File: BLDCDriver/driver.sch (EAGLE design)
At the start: 39 parts, among them Q1 NJM7800S, U1 QFN50P400X400X100-25NDRV8300D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, U2 AS5048A-HTSP-500, U4 SOP80P620X125-8N

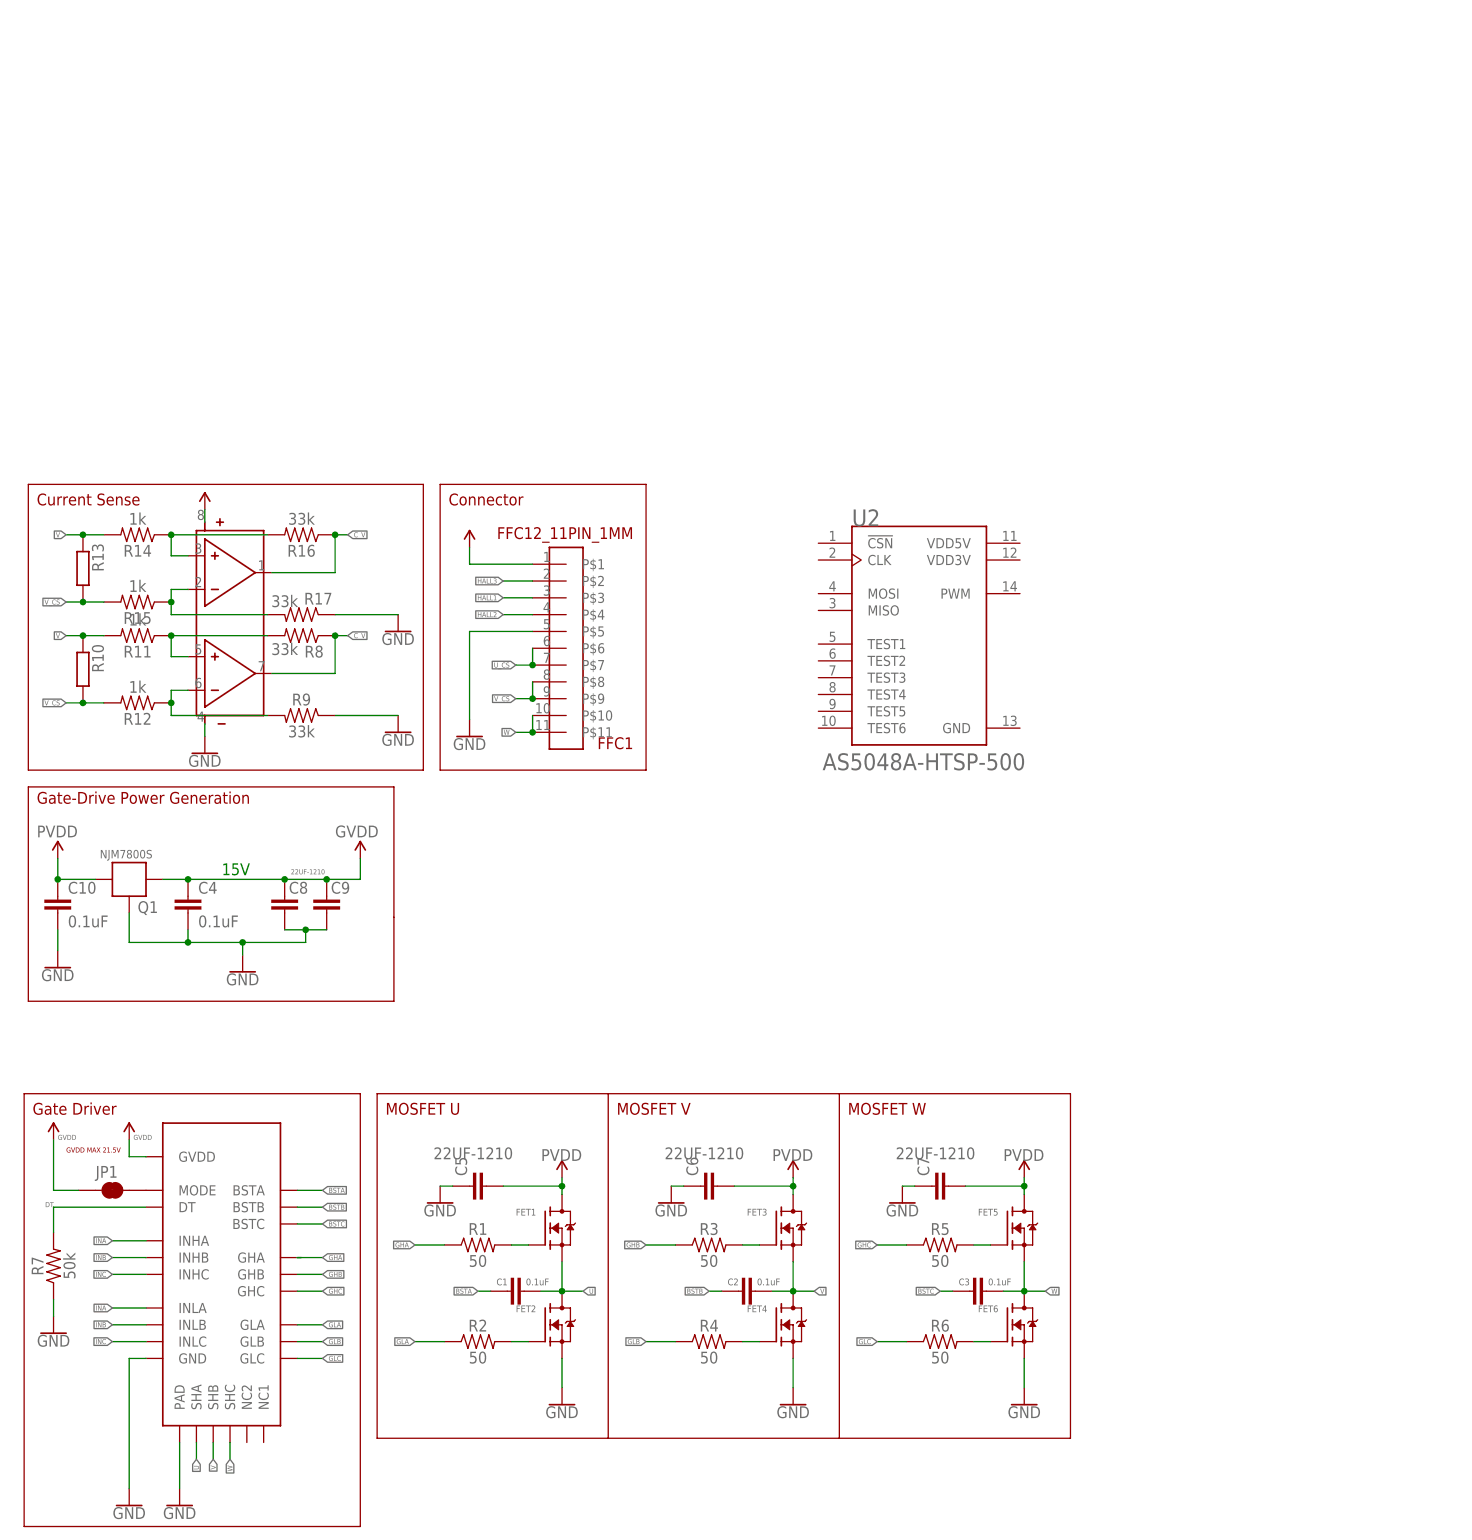
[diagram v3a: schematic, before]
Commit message: STM32と磁気エンコーダを追加した
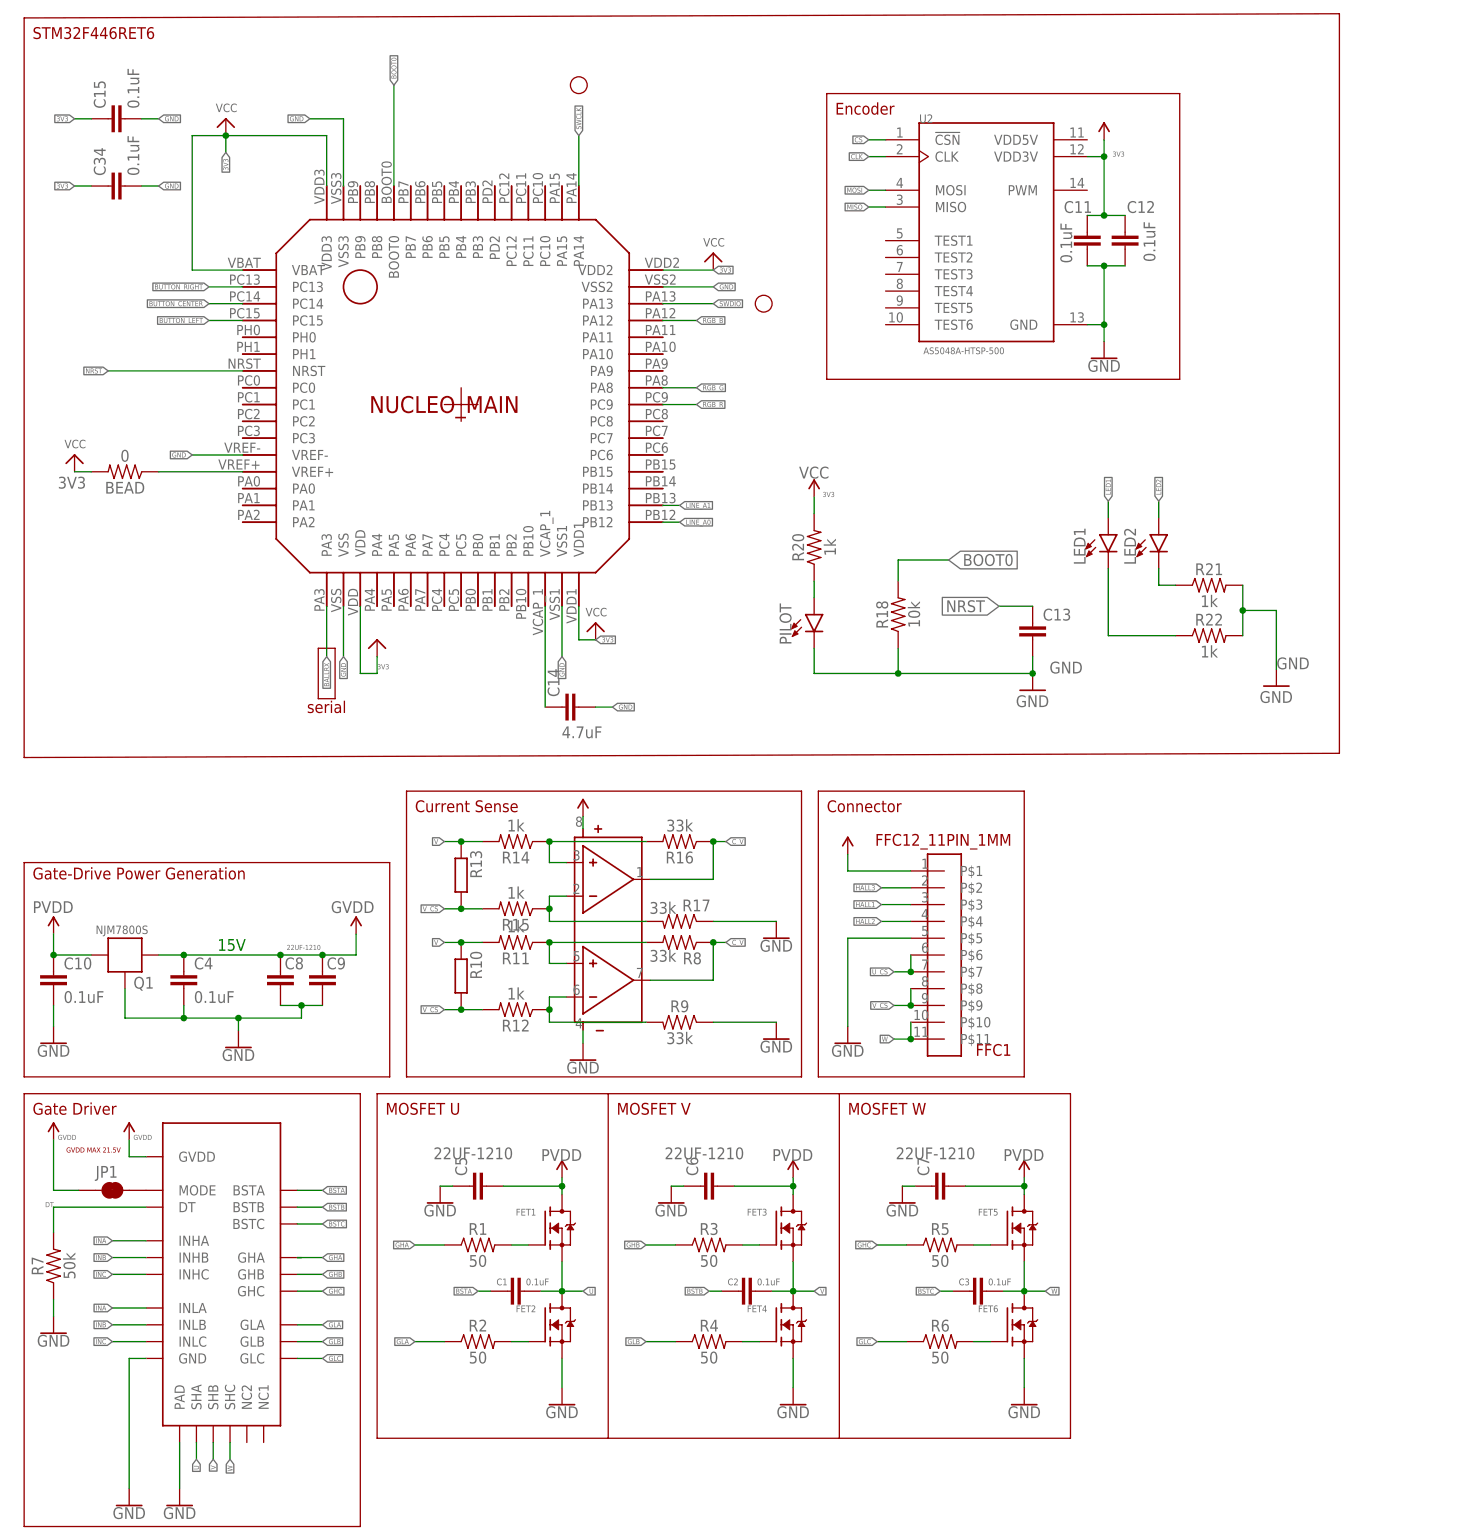
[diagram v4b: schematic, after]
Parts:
- added BEAD: 0, SparkFun-Resistors:0OHM-0603-1/10W-5%
- added C11, C12: 0.1uF, SparkFun-Capacitors:0.1UF-0603-100V-10%
- added C13: 0.1UF_1608, Custom_Designed_By_Yusei:0.1UF_1608
- added C14: 4.7uF, SparkFun-Capacitors:0.1UF-0603-25V-(+80/-20%)
- added C15, C34: 0.1uF, SparkFun-Capacitors:0.1UF-0603-25V-(+80/-20%)
- added LED1, LED2, PILOT: LED-SMD, Custom_Designed_By_Yusei:LED-SMD
- added NUCLEO_MAIN: F446RET6, STM32F446RET6:STM32F446RET6
- added R18: 10k, Custom_Designed_By_Yusei:RESISTOR-0603-1/10W-1%
- added R20, R21, R22: 1k, Custom_Designed_By_Yusei:RESISTOR-0603-1/10W-1%
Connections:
- new net BALLRX: NUCLEO_MAIN.PA3
- new net BOOT0: NUCLEO_MAIN.BOOT0, R18.2
- new net BUTTON_CENTER: NUCLEO_MAIN.PC14
- new net BUTTON_LEFT: NUCLEO_MAIN.PC15
- new net BUTTON_RIGHT: NUCLEO_MAIN.PC13
- new net CLK: U2.CLK
- new net CS: U2.!CSN
- new net LED1: LED1.A
- new net LED2: LED2.A
- new net LINE_A0: NUCLEO_MAIN.PB12
- new net LINE_A1: NUCLEO_MAIN.PB13
- new net MISO: U2.MISO
- new net MOSI: U2.MOSI
- new net N$12: LED2.C, R21.1
- new net N$13: LED1.C, R22.1
- new net NRST: C13.1, NUCLEO_MAIN.NRST
- new net POWERLED_RESISTOR: PILOT.A, R20.1
- new net RGB_B: NUCLEO_MAIN.PA12
- new net RGB_G: NUCLEO_MAIN.PA8
- new net RGB_R: NUCLEO_MAIN.PC9
- new net SWCLK: NUCLEO_MAIN.PA14
- new net SWDIO: NUCLEO_MAIN.PA13
- new net VCAP: C14.1, NUCLEO_MAIN.VCAP_1
- new net VDDA: BEAD.1, NUCLEO_MAIN.VREF+
- net 3V3: now also BEAD.2, C11.1, C12.1, C15.1, C34.1, NUCLEO_MAIN.VBAT, NUCLEO_MAIN.VDD, NUCLEO_MAIN.VDD1, NUCLEO_MAIN.VDD2, NUCLEO_MAIN.VDD3, R20.2, U2.VDD3V
- net GND: now also C11.2, C12.2, C13.2, C14.2, C15.2, C34.2, NUCLEO_MAIN.VREF-, NUCLEO_MAIN.VSS, NUCLEO_MAIN.VSS1, NUCLEO_MAIN.VSS2, NUCLEO_MAIN.VSS3, PILOT.C, R18.1, R21.2, R22.2, U2.GND
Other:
- note added: "Encoder"
- note added: "Recommended"
- note added: "STM32F446RET6"
- note added: "serial"
- moved on the sheet: C10, C4, C8, C9, FFC1, Q1, R10, R11, R12, R13, R14, R15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

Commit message: somefix
# ==== Emojis ====
# ✨ :sparkles: Add new feature
# ✅  :white_check_mark: Update existing feature (not bug)
# ⚠️  :warning: Fix bug/error
# 🔥  :fire: Remove files or features
# ✏️ :pencil2: Fix typos
# 📝  :memo: Update documentation
# ♻️  :recycle: Dependencies update
# 🐧  :penguin: Improved the Linux
# 🍎  :apple: Improved the macOS
# 🔖 :bookmark: Add new library
# 🎉  :tada: Initial commit

# ==== Format ====
# :emoji: Subject
#
# Commit body...

# ==== Messages ====
# 新規(ファイル)機能追加: Add
# 機能修正、既存機能追加（バグではない): Update
# リファクタリング: Clean
# ファイル名変更:
# 削除など: Remove
# バグ修正: Fix
# バージョンアップ: Upgrade
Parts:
- added C16: 22UF-1210, SparkFun-Capacitors:22UF-1210-16V-20%
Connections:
- net GND: now also C16.1
- net GVDD: now also C16.2
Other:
- moved on the sheet: C9
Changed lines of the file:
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@@
 <part name="P+6" library="audio amplifier example" library_urn="urn:adsk.eagle:library:970892" deviceset="VCC" device=""/>
 <part name="GND18" library="supply" deviceset="GND" device=""/>
+<part name="C16" library="SparkFun-Capacitors" deviceset="22UF" device="-1210-16V-20%" value="22UF-1210"/>
 </parts>
 <sheets>
@@
 <circle x="83.82" y="217.805" radius="1.27" width="0.1524" layer="94"/>
 <circle x="111.76" y="184.785" radius="1.27" width="0.1524" layer="94"/>
-<wire x1="0" y1="227.965" x2="0" y2="116.205" width="0.1524" layer="94"/>
-<wire x1="0" y1="116.205" x2="198.755" y2="116.84" width="0.1524" layer="94"/>
+<wire x1="0" y1="228.6" x2="0" y2="116.84" width="0.1524" layer="94"/>
+<wire x1="0" y1="116.84" x2="198.755" y2="116.84" width="0.1524" layer="94"/>
 <wire x1="198.755" y1="116.84" x2="198.755" y2="228.6" width="0.1524" layer="94"/>
-<wire x1="198.755" y1="228.6" x2="0" y2="227.965" width="0.1524" layer="94"/>
+<wire x1="198.755" y1="228.6" x2="0" y2="228.6" width="0.1524" layer="94"/>
 <text x="1.27" y="224.79" size="1.778" layer="94">STM32F446RET6</text>
 </plain>
@@
 <attribute name="VALUE" x="44.831" y="87.884" size="0.762" layer="96" font="vector" rot="R180"/>
 </instance>
-<instance part="C9" gate="G$1" x="45.085" y="83.82" smashed="yes" rot="R180">
-<attribute name="NAME" x="48.641" y="85.979" size="1.778" layer="95" font="vector" rot="R180"/>
+<instance part="C9" gate="G$1" x="44.45" y="83.82" smashed="yes" rot="R180">
+<attribute name="NAME" x="48.006" y="85.979" size="1.778" layer="95" font="vector" rot="R180"/>
 </instance>
 <instance part="GND6" gate="1" x="32.385" y="72.39" smashed="yes">
@@
 <instance part="GND18" gate="1" x="189.23" y="127" smashed="yes">
 <attribute name="VALUE" x="186.69" y="124.46" size="1.778" layer="96"/>
+</instance>
+<instance part="C16" gate="G$1" x="50.165" y="83.82" smashed="yes" rot="R180">
+<attribute name="NAME" x="53.721" y="85.979" size="1.778" layer="95" font="vector" rot="R180"/>
+<attribute name="VALUE" x="56.261" y="87.884" size="0.762" layer="96" font="vector" rot="R180"/>
 </instance>
 </instances>
@@
 <wire x1="15.24" y1="81.28" x2="15.24" y2="76.835" width="0.1524" layer="91"/>
 <pinref part="C4" gate="G$1" pin="2"/>
-<pinref part="C8" gate="G$1" pin="1"/>
-<pinref part="C9" gate="G$1" pin="1"/>
-<wire x1="38.735" y1="78.74" x2="41.91" y2="78.74" width="0.1524" layer="91"/>
-<wire x1="41.91" y1="78.74" x2="45.085" y2="78.74" width="0.1524" layer="91"/>
-<wire x1="41.91" y1="78.74" x2="41.91" y2="76.835" width="0.1524" layer="91"/>
-<junction x="41.91" y="78.74"/>
 <wire x1="24.13" y1="76.835" x2="24.13" y2="78.74" width="0.1524" layer="91"/>
 <wire x1="24.13" y1="76.835" x2="15.24" y2="76.835" width="0.1524" layer="91"/>
@@
 <pinref part="GND6" gate="1" pin="GND"/>
 <wire x1="24.13" y1="76.835" x2="32.385" y2="76.835" width="0.1524" layer="91"/>
-<wire x1="32.385" y1="76.835" x2="41.91" y2="76.835" width="0.1524" layer="91"/>
+<wire x1="32.385" y1="76.835" x2="44.45" y2="76.835" width="0.1524" layer="91"/>
 <wire x1="32.385" y1="74.93" x2="32.385" y2="76.835" width="0.1524" layer="91"/>
 <junction x="32.385" y="76.835"/>
+<pinref part="C9" gate="G$1" pin="1"/>
+<pinref part="C16" gate="G$1" pin="1"/>
+<wire x1="50.165" y1="78.74" x2="44.45" y2="78.74" width="0.1524" layer="91"/>
+<junction x="44.45" y="78.74"/>
+<pinref part="C8" gate="G$1" pin="1"/>
+<wire x1="38.735" y1="78.74" x2="44.45" y2="78.74" width="0.1524" layer="91"/>
+<wire x1="44.45" y1="78.105" x2="44.45" y2="78.74" width="0.1524" layer="91"/>
+<wire x1="44.45" y1="78.74" x2="44.45" y2="76.835" width="0.1524" layer="91"/>
 </segment>
 <segment>
@@
 <pinref part="C8" gate="G$1" pin="2"/>
 <junction x="38.735" y="86.36"/>
-<wire x1="38.735" y1="86.36" x2="45.085" y2="86.36" width="0.1524" layer="91"/>
+<wire x1="38.735" y1="86.36" x2="44.45" y2="86.36" width="0.1524" layer="91"/>
 <pinref part="C9" gate="G$1" pin="2"/>
-<junction x="45.085" y="86.36"/>
-<wire x1="45.085" y1="86.36" x2="50.165" y2="86.36" width="0.1524" layer="91"/>
+<junction x="44.45" y="86.36"/>
+<wire x1="44.45" y1="86.36" x2="50.165" y2="86.36" width="0.1524" layer="91"/>
 <wire x1="50.165" y1="86.36" x2="50.165" y2="89.535" width="0.1524" layer="91"/>
+<pinref part="C16" gate="G$1" pin="2"/>
+<junction x="50.165" y="86.36"/>
 </segment>
 </net>

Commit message: 自分、泣いていいすか
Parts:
- added C17: 0.1uF, Custom_Designed_By_Yusei:0.1UF_1608
- added C18: (no value), cap-pan40:C-PR-3,5X8
- added D1, D3, D4, D5, D6: WHITE, SparkFun-LED:LED-WHITE0603
- added D2: RED, SparkFun-LED:LED-RED0603
- added R19, R24, R25: 10k, SparkFun-Resistors:2.0KOHM-0603-1/10W-5%
- added R23, R26: 7k, SparkFun-Resistors:2.0KOHM-0603-1/10W-5%
- added R27: 8k, SparkFun-Resistors:2.0KOHM-0603-1/10W-5%
- added S1: SKRPACE010, Alps SW:SKRPACE010
- added STLINK: MAIN, jst-xh:B6B-XH-A
- added U$2: BAT, BAT:BAT
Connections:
- net BALLRX renamed USBRX
- removed net BUTTON_CENTER: NUCLEO_MAIN.PC14
- removed net BUTTON_LEFT: NUCLEO_MAIN.PC15
- removed net BUTTON_RIGHT: NUCLEO_MAIN.PC13
- removed net LINE_A0: NUCLEO_MAIN.PB12
- removed net LINE_A1: NUCLEO_MAIN.PB13
- removed net RGB_B: NUCLEO_MAIN.PA12
- removed net RGB_G: NUCLEO_MAIN.PA8
- removed net RGB_R: NUCLEO_MAIN.PC9
- new net C_U: NUCLEO_MAIN.PA0, R16.1, U4.O1
- new net LED: NUCLEO_MAIN.PC14, R23.2
- new net N$14: D1.A, R19.1
- new net N$15: D2.A, R27.1
- new net N$16: D3.A, R24.1
- new net N$17: D4.A, R25.1
- new net N$18: D5.A, R26.1
- new net N$21: D6.A, R23.1
- new net SW: NUCLEO_MAIN.PC13, S1.2
- new net USBTX: NUCLEO_MAIN.PA2, STLINK.1
- net 3V3: now also C17.1, STLINK.5
- net CLK: now also NUCLEO_MAIN.PA5
- net CS: now also NUCLEO_MAIN.PB6
- net C_V: now also NUCLEO_MAIN.PA1; no longer R16.1, U4.O1
- net GND: now also C17.2, C18.-, D1.C, D2.C, D3.C, D4.C, D5.C, D6.C, S1.4, STLINK.6, U$2.-
- net GVDD: now also R27.2
- net INA: now also NUCLEO_MAIN.PC7
- net INB: now also NUCLEO_MAIN.PB4
- net INC: now also NUCLEO_MAIN.PB10
- net MISO: now also NUCLEO_MAIN.PA6
- net MOSI: now also NUCLEO_MAIN.PA7
- net NRST: now also STLINK.2
- net PVDD: now also C18.+, R19.2, U$2.+
- net SWCLK: now also STLINK.4
- net SWDIO: now also STLINK.3
- net U: now also R13.2, R14.2, R24.2
- net U_CS: now also R13.1, R15.2
- net V: now also R25.2; no longer R13.2, R14.2
- net V_CS: no longer R13.1, R15.2
- net W: now also R26.2
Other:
- note removed: "serial"

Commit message: 救いはないんですか〜？
# ==== Emojis ====
# ✨ :sparkles: Add new feature
# ✅  :white_check_mark: Update existing feature (not bug)
# ⚠️  :warning: Fix bug/error
# 🔥  :fire: Remove files or features
# ✏️ :pencil2: Fix typos
# 📝  :memo: Update documentation
# ♻️  :recycle: Dependencies update
# 🐧  :penguin: Improved the Linux
# 🍎  :apple: Improved the macOS
# 🔖 :bookmark: Add new library
# 🎉  :tada: Initial commit

# ==== Format ====
# :emoji: Subject
#
# Commit body...

# ==== Messages ====
# 新規(ファイル)機能追加: Add
# 機能修正、既存機能追加（バグではない): Update
# リファクタリング: Clean
# ファイル名変更:
# 削除など: Remove
# バグ修正: Fix
# バージョンアップ: Upgrade
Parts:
- removed FET1, FET2, FET3, FET4, FET5, FET6: TPH11006NL, TPH11006NL:TPH11006NL
- added Q2, Q3, Q4: SIZ240DT-T1-GE3, SIZ240DT-T1-GE3:SIZ240DT-T1-GE3
- C2: value 0.1uF -> 22UF-1210; device SparkFun-Capacitors:0.1UF-0603-25V-5% -> SparkFun-Capacitors:22UF-1210-16V-20%
- C7: value 22UF-1210 -> 0.1uF; device SparkFun-Capacitors:22UF-1210-16V-20% -> SparkFun-Capacitors:0.1UF-0603-25V-5%
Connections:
- net BSTB: now also C3.1; no longer C2.1
- net BSTC: now also C7.1; no longer C3.1
- net GND: now also C2.1, Q2.S2, Q3.S2, Q4.S2; no longer C7.1, FET2.S, FET4.S, FET6.S
- net N$1: now also Q3.G1; no longer FET3.G
- net N$2: now also Q2.G1; no longer FET1.G
- net N$4: now also Q2.G2; no longer FET2.G
- net N$5: now also Q3.G2; no longer FET4.G
- net N$6: now also Q4.G1; no longer FET5.G
- net N$7: now also Q4.G2; no longer FET6.G
- net PVDD: now also C2.2, Q2.D1, Q3.D1, Q4.D1; no longer C7.2, FET1.D, FET3.D, FET5.D
- net U: now also Q2.S1/D2; no longer FET1.S, FET2.D
- net V: now also C3.2, Q3.S1/D2; no longer C2.2, FET3.S, FET4.D
- net W: now also C7.2, Q4.S1/D2; no longer C3.2, FET5.S, FET6.D
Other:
- moved on the sheet: C1, C18, C2, C3, C5, C6, C7, R1, R2, R3, R4, R5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
